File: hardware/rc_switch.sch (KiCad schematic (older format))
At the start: 9 parts, among them IC1 ATTINY85-P, P1 CONN_01X03, P2 CONN_01X04, P3 CONN_02X03, Q1 BUZ11, U1 ZTT8.00MT

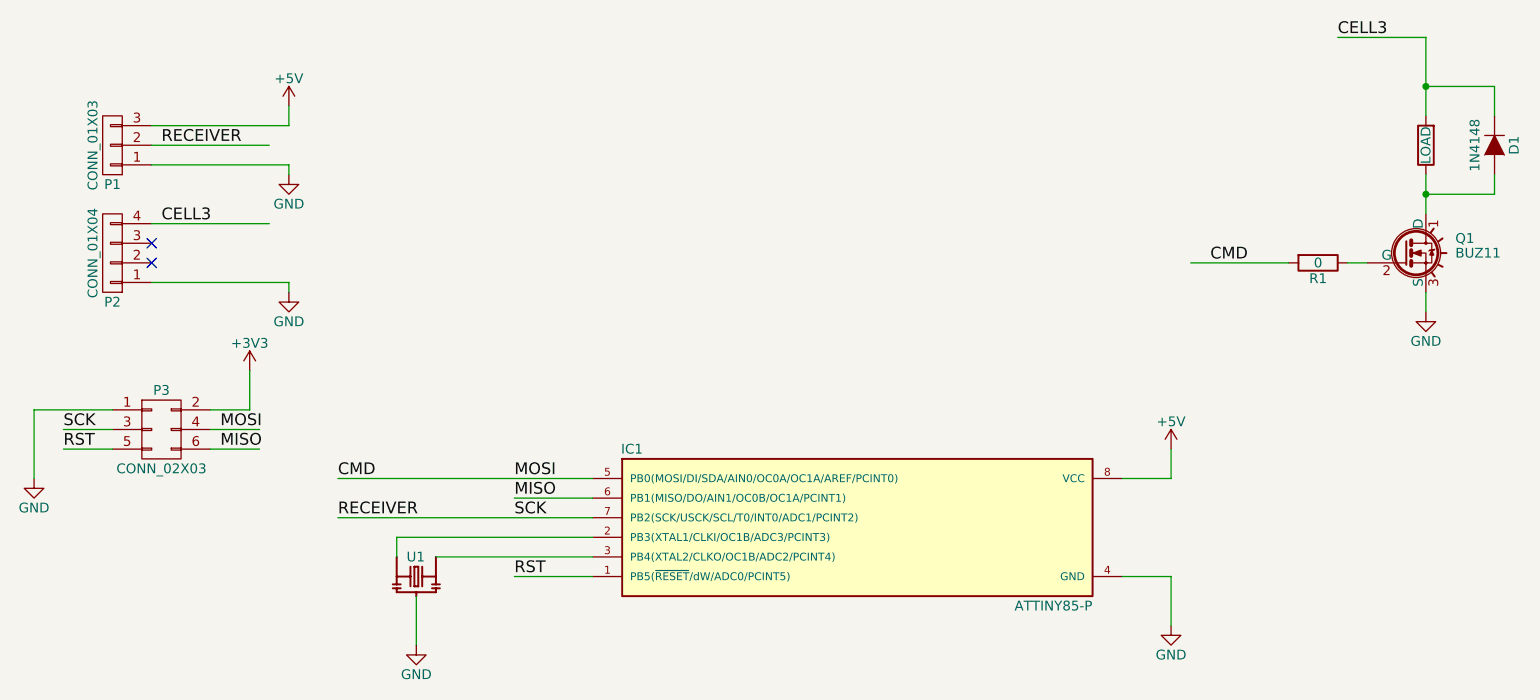
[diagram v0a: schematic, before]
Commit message: Removing some components to keep only the strictly necessary parts. Adding mounting holes.
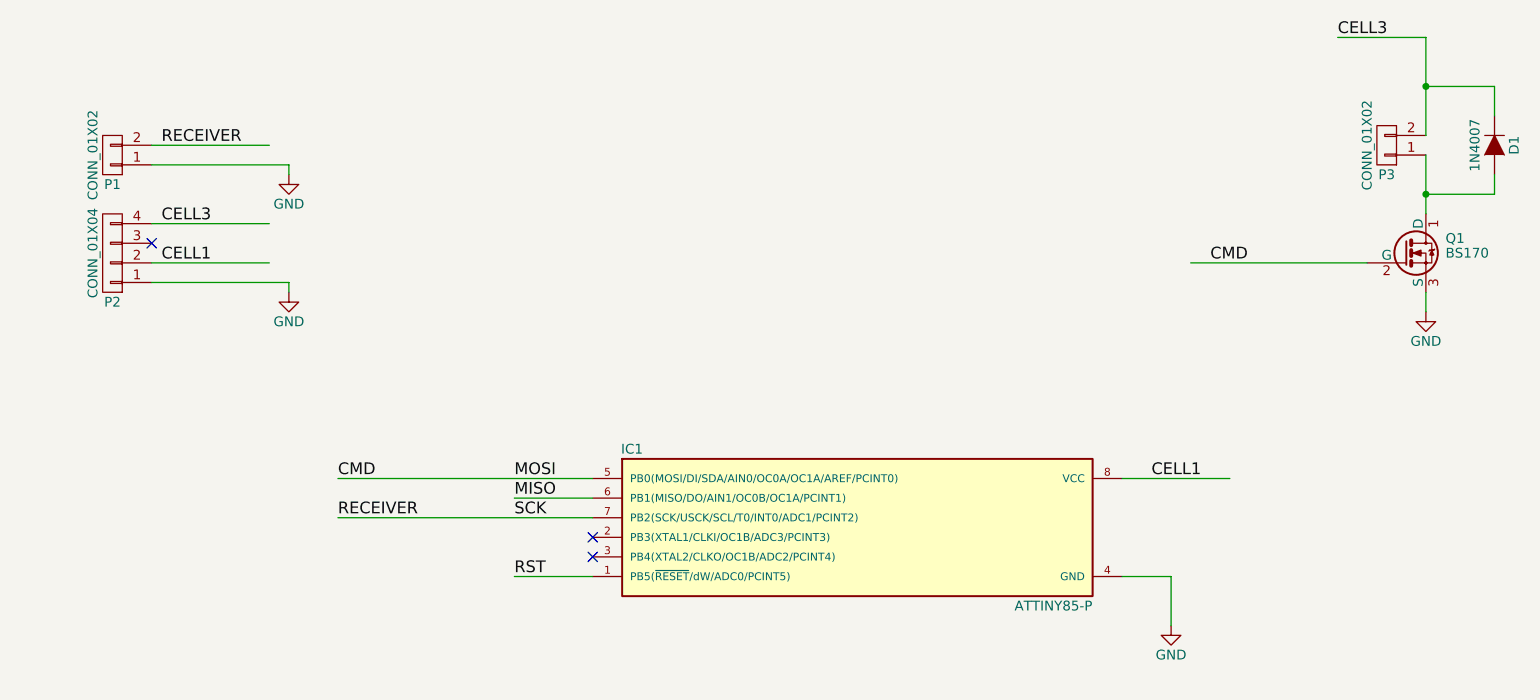
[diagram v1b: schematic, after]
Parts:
- removed P1: CONN_01X03, Socket_Strips:Socket_Strip_Straight_1x03, symbol CONN_01X03
- removed P3: CONN_02X03, Socket_Strips:Socket_Strip_Straight_1x06, symbol CONN_02X03
- removed Q1: BUZ11, TO-220, symbol BUZ11
- removed R1: 0, Resistors_ThroughHole:Resistor_Horizontal_RM7mm, symbol R
- removed R2: LOAD, Resistors_ThroughHole:Resistor_Horizontal_RM7mm, symbol R
- removed U1: ZTT8.00MT, ZTT8.00MT, symbol ZTT8.00MT
- added P1, P3: CONN_01X02, Socket_Strips:Socket_Strip_Straight_1x02, symbol CONN_01X02
- added Q1: BS170, TO_SOT_Packages_THT:TO-92_Inline_Wide, symbol BS170
- D1: value 1N4148 -> 1N4007
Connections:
- net labels added: CELL1
- net labels removed: +3V3, +5V
- wire segments 38 -> 23
- no-connect marks 2 -> 3
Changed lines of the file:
@@
 LIBS:valves
 LIBS:ZTT8.00MT
-LIBS:carte-cache
+LIBS:rc_switch-cache
 EELAYER 25 0
 EELAYER END
@@
 $EndComp
 $Comp
-L CONN_01X03 P1
-U 1 1 5986D88E
-P 1500 1600
-F 0 "P1" H 1500 1800 50  0000 C CNN
-F 1 "CONN_01X03" V 1600 1600 50  0000 C CNN
-F 2 "Socket_Strips:Socket_Strip_Straight_1x03" H 1500 1600 50  0001 C CNN
-F 3 "" H 1500 1600 50  0000 C CNN
-	1    1500 1600
-	-1   0    0    1
-$EndComp
-$Comp
 L CONN_01X04 P2
 U 1 1 5986D923
@@
 	1    0    0    -1
 $EndComp
-$Comp
-L +5V #PWR03
-U 1 1 5986DA5C
-P 2400 1400
-F 0 "#PWR03" H 2400 1250 50  0001 C CNN
-F 1 "+5V" H 2400 1540 50  0000 C CNN
-F 2 "" H 2400 1400 50  0000 C CNN
-F 3 "" H 2400 1400 50  0000 C CNN
-	1    2400 1400
-	1    0    0    -1
-$EndComp
 Text Label 1750 1600 0    60   ~ 0
 RECEIVER
 Text Label 1750 2000 0    60   ~ 0
 CELL3
-$Comp
-L +5V #PWR04
-U 1 1 5986DAD9
-P 6900 3150
-F 0 "#PWR04" H 6900 3000 50  0001 C CNN
-F 1 "+5V" H 6900 3290 50  0000 C CNN
-F 2 "" H 6900 3150 50  0000 C CNN
-F 3 "" H 6900 3150 50  0000 C CNN
-	1    6900 3150
-	1    0    0    -1
-$EndComp
-Wire Wire Line
-	1700 1500 2400 1500
 Wire Wire Line
 	1700 1600 2300 1600
@@
 	2400 1700 2400 1750
 Wire Wire Line
-	2400 1500 2400 1400
-Wire Wire Line
-	6650 3300 6900 3300
-Wire Wire Line
-	6900 3300 6900 3150
-$Comp
-L GND #PWR05
+	6650 3300 7200 3300
+$Comp
+L GND #PWR03
 U 1 1 5986DB1D
 P 6900 4050
-F 0 "#PWR05" H 6900 3800 50  0001 C CNN
+F 0 "#PWR03" H 6900 3800 50  0001 C CNN
 F 1 "GND" H 6900 3900 50  0000 C CNN
 F 2 "" H 6900 4050 50  0000 C CNN
@@
 	6900 3800 6650 3800
 $Comp
-L ZTT8.00MT U1
-U 1 1 5986DFD3
-P 3050 3800
-F 0 "U1" H 3000 3900 50  0000 L CNN
-F 1 "ZTT8.00MT" H 3050 3800 50  0001 L CNN
-F 2 "ZTT8.00MT" H 3050 3800 50  0001 L CNN
-F 3 "SIP-3 ECS International" H 3050 3800 50  0001 L CNN
-F 4 "ECS International" H 3050 3800 50  0001 L CNN "MF"
-F 5 "0.51 USD" H 3050 3800 50  0001 L CNN "Price"
-F 6 "Good" H 3050 3800 50  0001 L CNN "Availability"
-F 7 "Ceramic Resonators SIP-3 CER RES 8.0 MH" H 3050 3800 50  0001 L CNN "Description"
-F 8 "ZTT-8.00MT" H 3050 3800 50  0001 L CNN "MP"
-	1    3050 3800
-	1    0    0    -1
-$EndComp
-Wire Wire Line
-	3150 3700 3950 3700
-Wire Wire Line
-	3950 3600 2950 3600
-Wire Wire Line
-	2950 3600 2950 3700
-Wire Wire Line
-	3050 3900 3050 4150
-$Comp
-L GND #PWR06
-U 1 1 5986E076
-P 3050 4150
-F 0 "#PWR06" H 3050 3900 50  0001 C CNN
-F 1 "GND" H 3050 4000 50  0000 C CNN
-F 2 "" H 3050 4150 50  0000 C CNN
-F 3 "" H 3050 4150 50  0000 C CNN
-	1    3050 4150
-	1    0    0    -1
-$EndComp
-$Comp
-L BUZ11 Q1
-U 1 1 5986E0EE
-P 8100 2150
-F 0 "Q1" H 8350 2225 50  0000 L CNN
-F 1 "BUZ11" H 8350 2150 50  0000 L CNN
-F 2 "TO-220" H 8350 2075 50  0001 L CIN
-F 3 "" H 8100 2150 50  0000 L CNN
-	1    8100 2150
-	1    0    0    -1
-$EndComp
-$Comp
-L GND #PWR07
+L GND #PWR04
 U 1 1 5986E195
 P 8200 2450
-F 0 "#PWR07" H 8200 2200 50  0001 C CNN
+F 0 "#PWR04" H 8200 2200 50  0001 C CNN
 F 1 "GND" H 8200 2300 50  0000 C CNN
 F 2 "" H 8200 2450 50  0000 C CNN
@@
 Wire Wire Line
 	8200 2450 8200 2350
-$Comp
-L R R1
-U 1 1 5986E1F5
-P 7650 2200
-F 0 "R1" V 7730 2200 50  0000 C CNN
-F 1 "0" V 7650 2200 50  0000 C CNN
-F 2 "Resistors_ThroughHole:Resistor_Horizontal_RM7mm" V 7580 2200 50  0001 C CNN
-F 3 "" H 7650 2200 50  0000 C CNN
-	1    7650 2200
-	0    1    1    0
-$EndComp
-Wire Wire Line
-	7800 2200 7900 2200
-Wire Wire Line
-	7000 2200 7500 2200
+Wire Wire Line
+	7000 2200 7900 2200
 Text Label 7100 2200 0    60   ~ 0
 CMD
-$Comp
-L R R2
-U 1 1 5986E2DE
-P 8200 1600
-F 0 "R2" V 8280 1600 50  0001 C CNN
-F 1 "LOAD" V 8200 1600 50  0000 C CNN
-F 2 "Resistors_ThroughHole:Resistor_Horizontal_RM7mm" V 8130 1600 50  0001 C CNN
-F 3 "" H 8200 1600 50  0000 C CNN
-	1    8200 1600
-	-1   0    0    1
-$EndComp
 $Comp
 L D D1
@@
 P 8550 1600
 F 0 "D1" H 8550 1700 50  0000 C CNN
-F 1 "1N4148" H 8550 1500 50  0000 C CNN
+F 1 "1N4007" H 8550 1500 50  0000 C CNN
 F 2 "Diodes_ThroughHole:Diode_DO-35_SOD27_Horizontal_RM10" H 8550 1600 50  0001 C CNN
 F 3 "" H 8550 1600 50  0000 C CNN
@@
 $EndComp
 Wire Wire Line
-	8200 1750 8200 1950
+	8200 1650 8200 1950
 Wire Wire Line
 	8550 1750 8550 1850
@@
 	8550 1300 8200 1300
 Wire Wire Line
-	8200 1050 8200 1450
+	8200 1050 8200 1550
 Wire Wire Line
 	2650 3500 3950 3500
 Text Label 2650 3500 0    60   ~ 0
 RECEIVER
-$Comp
-L CONN_02X03 P3
-U 1 1 5986ED3D
-P 1750 3050
-F 0 "P3" H 1750 3250 50  0000 C CNN
-F 1 "CONN_02X03" H 1750 2850 50  0000 C CNN
-F 2 "Socket_Strips:Socket_Strip_Straight_1x06" H 1750 2750 50  0001 C CNN
-F 3 "" H 1750 1850 50  0000 C CNN
-	1    1750 3050
-	1    0    0    -1
-$EndComp
-$Comp
-L GND #PWR08
-U 1 1 5986EEF2
-P 1100 3300
-F 0 "#PWR08" H 1100 3050 50  0001 C CNN
-F 1 "GND" H 1100 3150 50  0000 C CNN
-F 2 "" H 1100 3300 50  0000 C CNN
-F 3 "" H 1100 3300 50  0000 C CNN
-	1    1100 3300
-	1    0    0    -1
-$EndComp
-Wire Wire Line
-	1500 3050 1250 3050
-Wire Wire Line
-	1500 3150 1250 3150
-Wire Wire Line
-	1100 3300 1100 2950
-Wire Wire Line
-	1100 2950 1500 2950
-Text Label 1250 3050 0    60   ~ 0
-SCK
-Text Label 1250 3150 0    60   ~ 0
-RST
-$Comp
-L +3V3 #PWR09
-U 1 1 5986EFBE
-P 2200 2750
-F 0 "#PWR09" H 2200 2600 50  0001 C CNN
-F 1 "+3V3" H 2200 2890 50  0000 C CNN
-F 2 "" H 2200 2750 50  0000 C CNN
-F 3 "" H 2200 2750 50  0000 C CNN
-	1    2200 2750
-	1    0    0    -1
-$EndComp
-Wire Wire Line
-	2000 2950 2200 2950
-Wire Wire Line
-	2200 2950 2200 2750
-Wire Wire Line
-	2000 3050 2250 3050
-Wire Wire Line
-	2250 3150 2000 3150
-Text Label 2050 3050 0    60   ~ 0
-MOSI
-Text Label 2050 3150 0    60   ~ 0
-MISO
 Wire Wire Line
 	2650 3300 3950 3300
@@
 RST
 NoConn ~ 1700 2100
-NoConn ~ 1700 2200
+$Comp
+L CONN_01X02 P1
+U 1 1 598CC06C
+P 1500 1650
+F 0 "P1" H 1500 1800 50  0000 C CNN
+F 1 "CONN_01X02" V 1600 1650 50  0000 C CNN
+F 2 "Socket_Strips:Socket_Strip_Straight_1x02" H 1500 1650 50  0001 C CNN
+F 3 "" H 1500 1650 50  0000 C CNN
+	1    1500 1650
+	-1   0    0    1
+$EndComp
+$Comp
+L BS170 Q1
+U 1 1 598CC346
+P 8100 2150
+F 0 "Q1" H 8300 2225 50  0000 L CNN
+F 1 "BS170" H 8300 2150 50  0000 L CNN
+F 2 "TO_SOT_Packages_THT:TO-92_Inline_Wide" H 8300 2075 50  0001 L CIN
+F 3 "" H 8100 2150 50  0000 L CNN
+	1    8100 2150
+	1    0    0    -1
+$EndComp
+$Comp
+L CONN_01X02 P3
+U 1 1 598CC596
+P 8000 1600
+F 0 "P3" H 8000 1750 50  0000 C CNN
+F 1 "CONN_01X02" V 8100 1600 50  0000 C CNN
+F 2 "Socket_Strips:Socket_Strip_Straight_1x02" H 8000 1600 50  0001 C CNN
+F 3 "" H 8000 1600 50  0000 C CNN
+	1    8000 1600
+	-1   0    0    1
+$EndComp
+Text Label 6800 3300 0    60   ~ 0
+CELL1
+NoConn ~ 3950 3600
+NoConn ~ 3950 3700
+Wire Wire Line
+	1700 2200 2300 2200
+Text Label 1750 2200 0    60   ~ 0
+CELL1
 $EndSCHEMATC
